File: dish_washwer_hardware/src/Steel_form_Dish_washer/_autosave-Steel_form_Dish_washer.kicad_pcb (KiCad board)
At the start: 2 copper layers, 230 x 287 mm, 143 parts, among them J1 RTD_TANK_SENSOR, J10 DRAIN PUMP CONNECTOR, J11 WASH PUMP CONNECTOR, J12 BOILER HEATER CONNECTOR, J13 TANK HEATER, J14 peristaltic_pump_2, J15 peristaltic_pump_1, J16 SCREEN CONNECTOR, J17 Conn_02x06_Odd_Even, J18 Conn_02x06_Odd_Even, J2 RTD_BOILER_SENSOR, J3 AC_PWR_IN, J4 MAG_DOOR_SENSOR, J5 Conn_02x03_Odd_Even, J6 Conn_01x04_Male, J7 BOILER HEATER CONNECTOR, J8 Conn_01x10_Male, J9 SOLENOID CONNECTOR, K1 9-1440003-0, K2 9-1440003-0, K3 9-1440003-0, K4 9-1440003-0, Q3 WST2N7002K, Q4 WST2N7002K, Q5 WST2N7002K, SW1 SW_Push, U1 ATmega2560-16AU, U10 MOC3021, U11 MOC3021, U12 MOC3021, U13 EL817, U14 9-1393243-3, U15 TXS0108EPW, U16 EAST1616RGBA8, U17 EAST1616RGBA8, U18 MPR121QR2, U2 LM1117-3.3, U3 MAX31865ATP+T, U4 MAX31865ATP+T, U5 9-1393243-3, U6 HCPL3700M, U7 MOC3021, U8 MOC3021, U9 MOC3021, Y1 C3E-16.000-12-1010-M

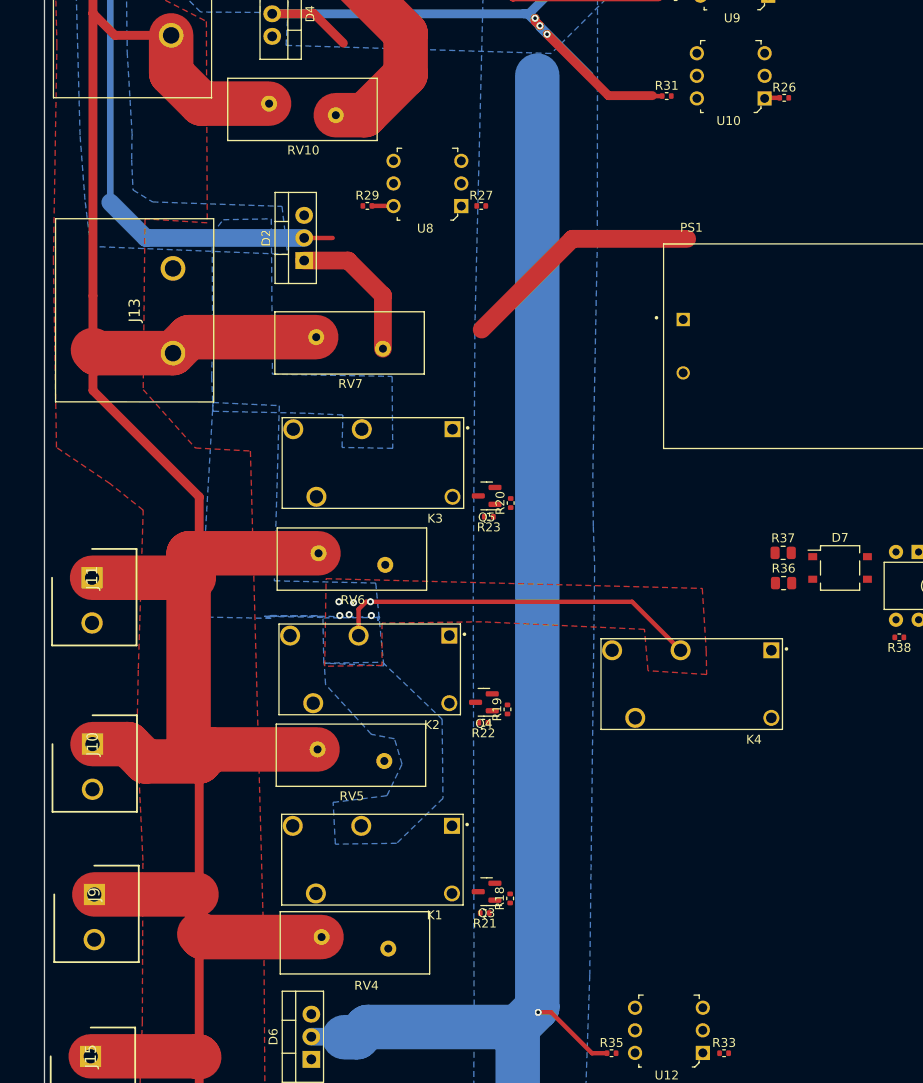
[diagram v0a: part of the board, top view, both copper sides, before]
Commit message: updated layout
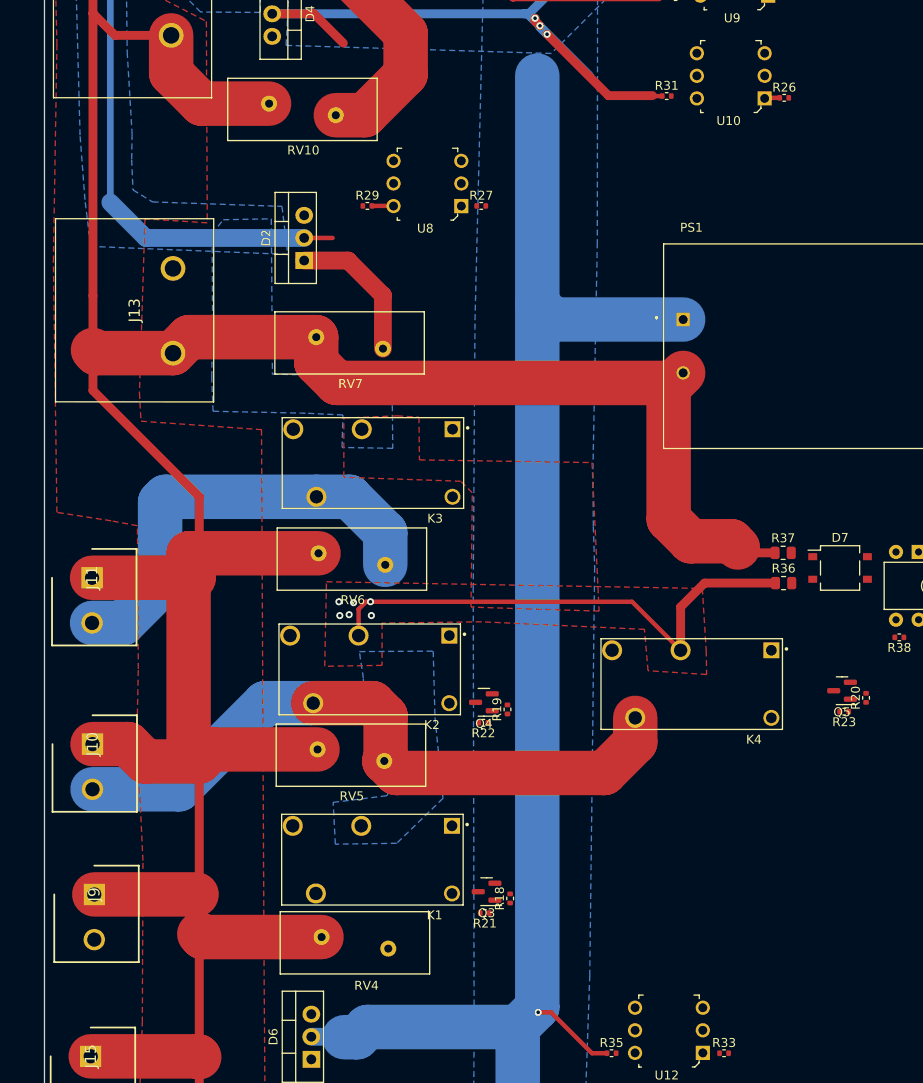
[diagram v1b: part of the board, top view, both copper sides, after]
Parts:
- moved R20 45.6 mm to (161.7, 187.0)
- moved Q5 45.6 mm to (159.0, 186.2)
- moved R23 45.6 mm to (159.2, 188.6)
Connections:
- PS1 pad 1: L1 -> L3
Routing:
- net /AC_ACTUATORS/DRAIN_CONN+: track 0.00 -> 75.6 mm
- net NEUTRAL: track 558.4 -> 632.6 mm
- net Net-(J11-Pad2): track 0.00 -> 49.7 mm
- net L3: track 346.8 -> 363.9 mm
- net L1: track 275.7 -> 265.0 mm
